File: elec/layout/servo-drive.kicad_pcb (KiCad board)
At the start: 2 copper layers, 80 parts

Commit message: layout done
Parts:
- U16: renamed from A13; footprint Connector_Wire:SolderWirePad_1x01_SMD_1x2mm -> Connector_Wire:SolderWirePad_1x01_SMD_5x10mm
- U17: renamed from A14; footprint Connector_Wire:SolderWirePad_1x01_SMD_1x2mm -> Connector_Wire:SolderWirePad_1x01_SMD_5x10mm
- U18: renamed from A15; footprint Connector_Wire:SolderWirePad_1x01_SMD_1x2mm -> Connector_Wire:SolderWirePad_1x01_SMD_5x10mm
- U4: renamed from A1; footprint Connector_Wire:SolderWirePad_1x01_SMD_1x2mm -> Connector_Wire:SolderWirePad_1x01_SMD_5x10mm
- U7: renamed from A4; footprint Connector_Wire:SolderWirePad_1x01_SMD_1x2mm -> Connector_Wire:SolderWirePad_1x01_SMD_5x10mm
- moved U27 132.2 mm to (99.6, 62.5), turned to 180 degrees
- moved U11 92.1 mm to (104.8, 54.9)
- moved U24 81.9 mm to (93.5, 77.2), turned to 180 degrees
- moved U1 81.7 mm to (91.3, 80.3), turned to 90 degrees
- moved U12 79.0 mm to (116.5, 54.6)
- moved U13 71.9 mm to (120.0, 54.6)
- moved U20 70.5 mm to (129.8, 54.1)
- moved U15 69.7 mm to (150.9, 54.9)
- moved U2 65.9 mm to (114.8, 80.4), turned to 90 degrees
- moved U16 64.1 mm to (98.0, 99.6)
- moved U25 63.6 mm to (117.3, 77.2)
- moved R2 63.1 mm to (139.4, 53.3), turned to 180 degrees
- moved R20 61.6 mm to (97.5, 69.3), turned to -90 degrees
- moved U19 60.7 mm to (142.7, 56.4)
- moved U10 59.6 mm to (101.2, 54.9)
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- renumbered C4 to C1, C12 to C10, C13 to C11, C1 to C12, C2 to C13, C3 to C14, C14 to C2, C5 to C3, C6 to C4, C7 to C5, C8 to C6, C9 to C7, C10 to C8, C11 to C9, R22 to R1, R19 to R10, R20 to R11, R21 to R12, R25 to R13, R26 to R14, R27 to R15, R28 to R16, R29 to R17, R30 to R18, R1 to R19, R23 to R2, R2 to R20, R3 to R21, R4 to R22, R5 to R23, R6 to R24, R7 to R25, R8 to R26, R9 to R27, R10 to R28, R11 to R29, R24 to R3, R12 to R30, R13 to R4, R14 to R5, R15 to R6, R16 to R7, R17 to R8, R18 to R9, U5 to U1, A7 to U10, A8 to U11, A9 to U12, A10 to U13, A11 to U14, A12 to U15, A16 to U19, U6 to U2, A17 to U20, A18 to U21, A19 to U22, A20 to U23, A21 to U24, A22 to U25, A23 to U26, U1 to U27, U2 to U28, U3 to U29, U7 to U3, U4 to U30, A2 to U5, A3 to U6, A5 to U8, A6 to U9
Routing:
- net 16: track 0.00 -> 114.2 mm
- net 3: track 0.00 -> 78.6 mm, vias 0 -> 4
- net 4: track 0.00 -> 55.8 mm
- net 5: track 0.00 -> 43.6 mm, vias 0 -> 58
- net 24: track 0.00 -> 29.0 mm
- net 40: track 0.00 -> 29.0 mm
- net 56: track 0.00 -> 28.1 mm
- net 13: track 0.00 -> 20.0 mm
- net 14: track 0.00 -> 20.0 mm
- net 106: track 0.00 -> 19.3 mm
- net 95: track 0.00 -> 19.1 mm
- net 63: track 0.00 -> 17.9 mm
- net 12: track 0.00 -> 17.8 mm
- net 47: track 0.00 -> 17.7 mm
- net 85: track 0.00 -> 17.0 mm
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- added copper zone on B.Cu, net 2
- added copper zone on F.Cu, net 2
- added copper zone on F.Cu, net 24
- added copper zone on F.Cu, net 40
- added copper zone on F.Cu, net 5
- added copper zone on In1.Cu, net 5
- added copper zone on F.Cu, net 56
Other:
- board outline added: 85.3 x 55.9 mm
- copper layers 2 -> 4
- board text added: "10V"
- board text added: "3v3"
- board text added: "<26V"
- board text added: "GND"

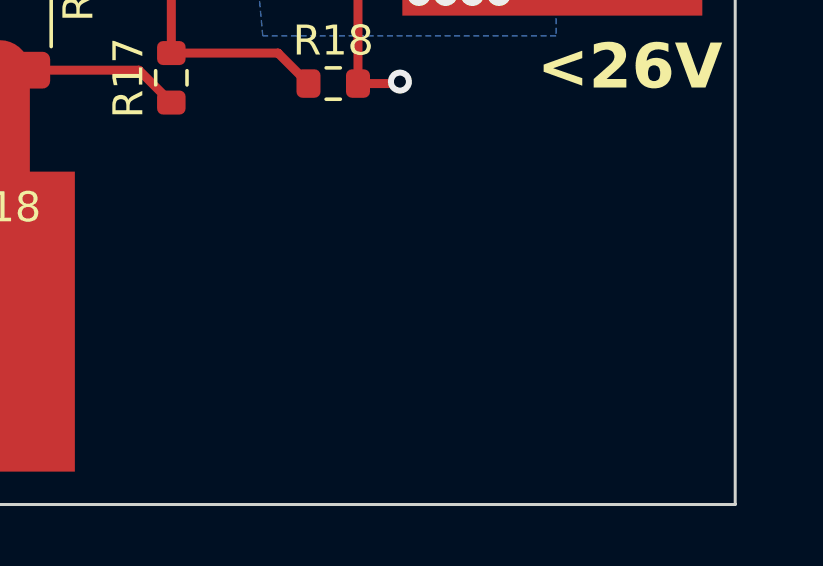
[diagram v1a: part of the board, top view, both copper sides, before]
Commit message: add githash to board
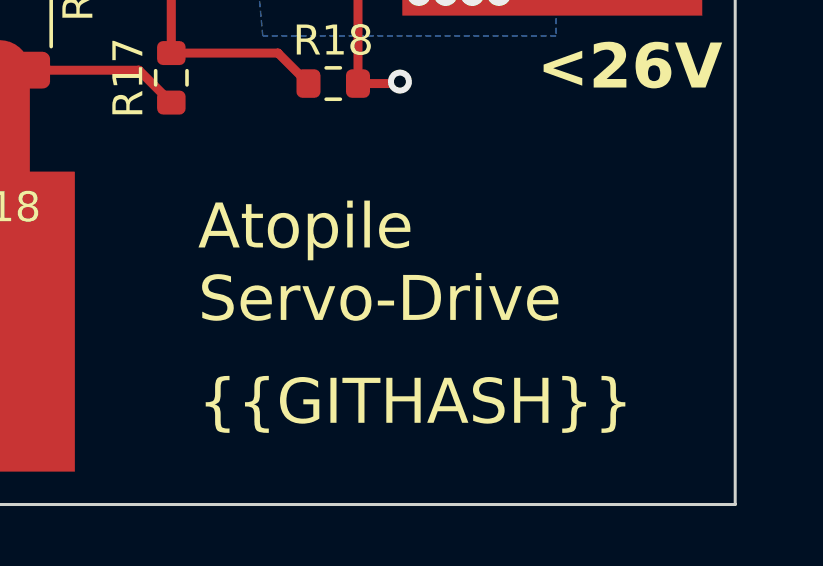
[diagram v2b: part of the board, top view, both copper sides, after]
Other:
- board text added: "Atopile Servo-Drive"
- board text added: "{{GITHASH}}"
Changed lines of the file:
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@@
     (effects (font (size 1.5 1.5) (thickness 0.3) bold) (justify left bottom))
+  )
+  (gr_text "{{GITHASH}}" (at 153.289 103.124) (layer "F.SilkS")
+    (effects (font (size 1.5 1.5) (thickness 0.15)) (justify left bottom))
+  )
+  (gr_text "Atopile\nServo-Drive" (at 153.289 99.695) (layer "F.SilkS")
+    (effects (font (size 1.5 1.5) (thickness 0.15)) (justify left bottom))
   )
   (gr_text "<26V" (at 164.592 91.948) (layer "F.SilkS")

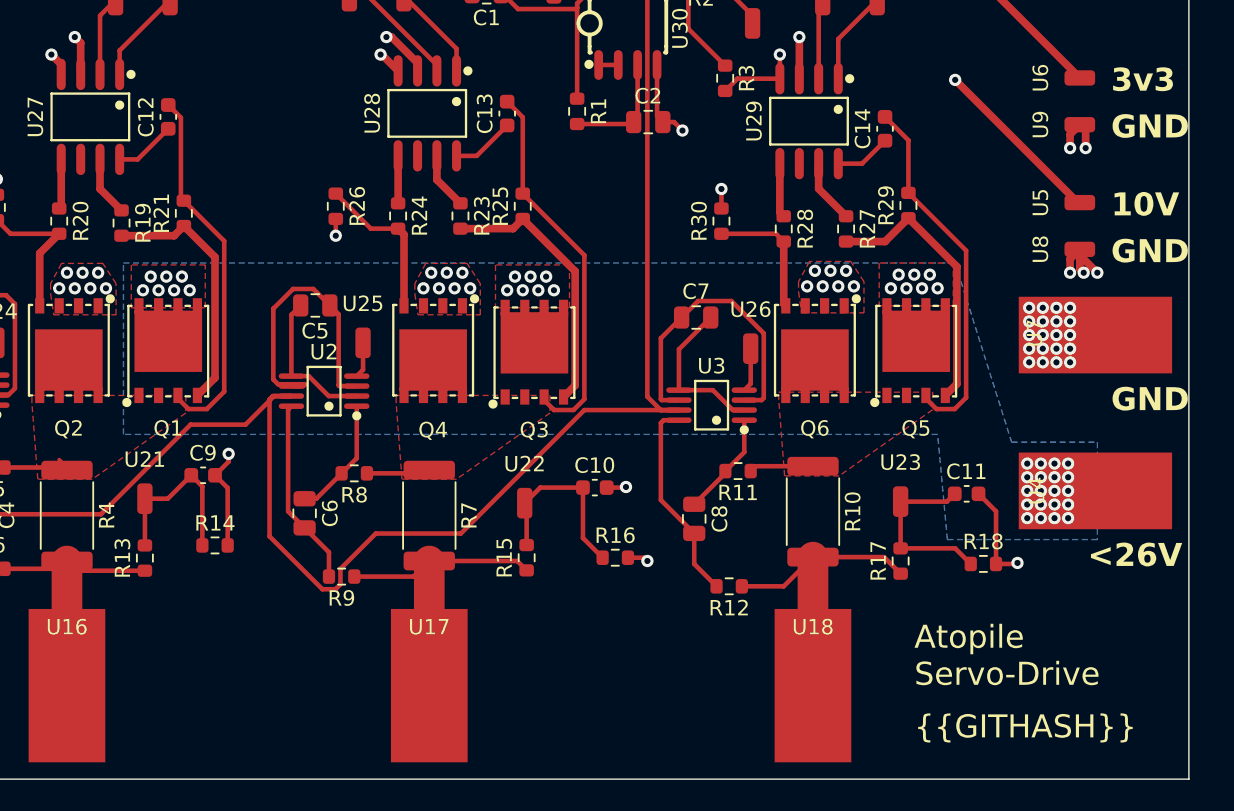
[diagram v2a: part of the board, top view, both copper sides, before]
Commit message: add bypass caps to power rail
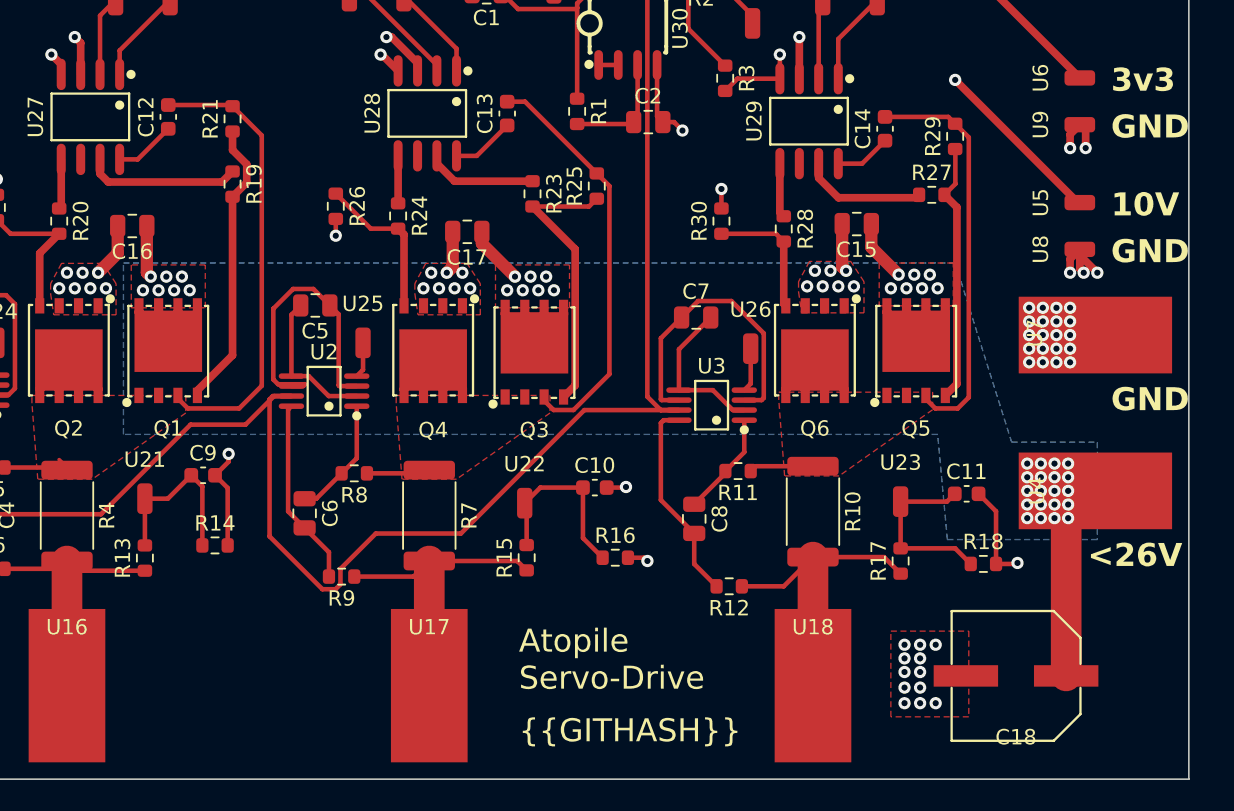
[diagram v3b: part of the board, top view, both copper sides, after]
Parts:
- added C15: 4.7uF, Capacitor_SMD:C_0805_2012Metric, F.Cu at (149.5, 69.5)
- added C16: 4.7uF, Capacitor_SMD:C_0805_2012Metric, F.Cu at (102.3, 69.6)
- added C17: 4.7uF, Capacitor_SMD:C_0805_2012Metric, F.Cu at (124.1, 70.0)
- added C18: 100uF, lib:CAP-SMD_BD8.0-L8.3-W8.3-FD, F.Cu at (159.9, 98.9)
- moved R19 7.67 mm to (108.8, 66.9)
- moved R21 6.93 mm to (108.8, 62.6)
- moved R27 6.01 mm to (154.4, 67.6), turned to 0 degrees
- moved R29 5.44 mm to (156.0, 63.8)
- moved R25 5.00 mm to (132.6, 67.0)
- moved R23 4.92 mm to (128.4, 67.5)
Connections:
- net 24 renamed 25
- net 43 renamed 46
- net 49 renamed 52
- net 58 renamed 62
- net 60 renamed 64
- net 73 renamed 77
- net 74 renamed 78
- net 75 renamed 79
- C12 pad 1: 27 -> 29
- C13 pad 2: 40 -> 42
- C14 pad 1: 59 -> 63
- C14 pad 2: 56 -> 59
- C3 pad 1: 84 -> 88
- C3 pad 2: 85 -> 89
- C4 pad 1: 88 -> 92
- C4 pad 2: 89 -> 93
- C5 pad 1: 95 -> 99
- C5 pad 2: 96 -> 100
- C6 pad 1: 99 -> 103
- C6 pad 2: 100 -> 104
- C7 pad 1: 106 -> 110
- C7 pad 2: 107 -> 111
- C8 pad 1: 110 -> 114
- C8 pad 2: 111 -> 115
- Q1 pad 4: 31 -> 33
- Q2 pad 4: 33 -> 35
- Q3 pad 1: 40 -> 42
- Q3 pad 2: 40 -> 42
- Q3 pad 3: 40 -> 42
- Q3 pad 4: 47 -> 50
- Q4 pad 5: 40 -> 42
- Q4 pad 6: 40 -> 42
- Q4 pad 7: 40 -> 42
- Q4 pad 8: 40 -> 42
- Q4 pad 9: 40 -> 42
- Q5 pad 1: 56 -> 59
- Q5 pad 2: 56 -> 59
- Q5 pad 3: 56 -> 59
- Q5 pad 4: 63 -> 67
- Q6 pad 4: 65 -> 69
- Q6 pad 5: 56 -> 59
- Q6 pad 6: 56 -> 59
- Q6 pad 7: 56 -> 59
- Q6 pad 8: 56 -> 59
- Q6 pad 9: 56 -> 59
- R10 pad 1: 56 -> 59
- R11 pad 1: 56 -> 59
- R11 pad 2: 110 -> 114
- R12 pad 2: 111 -> 115
- R19 pad 1: 26 -> 28
- R19 pad 2: 31 -> 33
- R20 pad 1: 29 -> 31
- R20 pad 2: 33 -> 35
- R21 pad 1: 31 -> 33
- R22 pad 1: 33 -> 35
- R23 pad 1: 42 -> 45
- R23 pad 2: 47 -> 50
- R24 pad 1: 45 -> 48
- R25 pad 1: 47 -> 50
- R25 pad 2: 40 -> 42
- R27 pad 2: 63 -> 67
- R28 pad 1: 61 -> 65
- R28 pad 2: 65 -> 69
- R29 pad 1: 63 -> 67
- R29 pad 2: 56 -> 59
- R30 pad 1: 65 -> 69
- R5 pad 2: 88 -> 92
- R6 pad 2: 89 -> 93
- R7 pad 1: 40 -> 42
- R8 pad 1: 40 -> 42
- R8 pad 2: 99 -> 103
- R9 pad 2: 100 -> 104
- U1 pad 1: 88 -> 92
- U1 pad 2: 85 -> 89
- U1 pad 3: 84 -> 88
- U1 pad 5: 85 -> 89
- U1 pad 6: 84 -> 88
- U1 pad 8: 89 -> 93
- U2 pad 1: 99 -> 103
- U2 pad 2: 96 -> 100
- U2 pad 3: 95 -> 99
- U2 pad 5: 96 -> 100
- U2 pad 6: 95 -> 99
- U2 pad 8: 100 -> 104
- U27 pad 5: 29 -> 31
- U27 pad 6: 28 -> 30
- U27 pad 7: 26 -> 28
- U27 pad 8: 27 -> 29
- U28 pad 5: 45 -> 48
- U28 pad 6: 44 -> 47
- U28 pad 7: 42 -> 45
- U29 pad 5: 61 -> 65
- U29 pad 8: 59 -> 63
- U3 pad 1: 110 -> 114
- U3 pad 2: 107 -> 111
- U3 pad 3: 106 -> 110
- U3 pad 5: 107 -> 111
- U3 pad 6: 106 -> 110
- U3 pad 8: 111 -> 115
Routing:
- net 40: track 29.0 -> 0.00 mm
- net 56: track 28.1 -> 0.00 mm
- net 42: track 3.73 -> 31.1 mm
- net 59: track 3.67 -> 30.7 mm
- net 2: track 0.00 -> 24.1 mm
- net 106: track 19.3 -> 0.00 mm
- net 95: track 19.1 -> 0.00 mm
- net 50: track 0.00 -> 18.3 mm
- net 47: track 17.7 -> 0.00 mm
- net 67: track 0.00 -> 17.0 mm
- net 85: track 17.0 -> 0.00 mm
- net 63: track 17.9 -> 3.67 mm
- net 31: track 16.7 -> 3.25 mm
- net 115: track 0.00 -> 13.4 mm
- net 93: track 0.00 -> 13.0 mm
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- added copper zone on F.Cu, net 42
- added copper zone on F.Cu, net 59
- removed copper zone on F.Cu, net 40
- removed copper zone on F.Cu, net 56
